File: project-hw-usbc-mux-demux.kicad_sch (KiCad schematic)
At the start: 0 parts

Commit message: sch: add buck converter
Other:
- added sheet Buck Converter (buck_converter.kicad_sch)
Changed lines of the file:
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@@
 	(generator_version "8.0")
 	(paper "A4")
+	(sheet
+		(at 38.735 38.1)
+		(size 14.605 12.7)
+		(fields_autoplaced yes)
+		(stroke
+			(width 0.1524)
+			(type solid)
+		)
+		(fill
+			(color 0 0 0 0.0000)
+		)
+		(property "Sheetname" "Buck Converter"
+			(at 38.735 37.3884 0)
+			(effects
+				(font
+					(size 1.27 1.27)
+				)
+				(justify left bottom)
+			)
+		)
+		(property "Sheetfile" "buck_converter.kicad_sch"
+			(at 38.735 51.3846 0)
+			(effects
+				(font
+					(size 1.27 1.27)
+				)
+				(justify left top)
+			)
+		)
+		(pin "5V" output
+			(at 53.34 40.64 0)
+			(effects
+				(font
+					(size 1.27 1.27)
+				)
+				(justify right)
+			)
+		)
+		(pin "Vin" input
+			(at 38.735 40.64 180)
+			(effects
+				(font
+					(size 1.27 1.27)
+				)
+				(justify left)
+			)
+		)
+		(pin "GND" input
+			(at 38.735 48.26 180)
+			(effects
+				(font
+					(size 1.27 1.27)
+				)
+				(justify left)
+			)
+		)
+		(instances
+			(project "project-hw-usbc-mux-demux"
+				(path "/a3c0ab3f-ca32-4edb-a5c1-d200028ec7dc"
+					(page "2")
+				)
+			)
+		)
+	)
 	(sheet_instances
 		(path "/"

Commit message: sch: first draft
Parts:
- added D1: LED_Small, LED_SMD:LED_0603_1608Metric, symbol Device:LED_Small
- added J1, J2, J3: Amphenol_12402012E212A, symbol Amphenol_12402012E212A:Amphenol_12402012E212A
- added R5, R6: 10k, Resistor_SMD:R_0603_1608Metric, symbol Device:R_Small
- added R7: 1k, Resistor_SMD:R_0603_1608Metric, symbol Device:R_Small
- added U2: FUSB303BTMX, QFN:Texas_X2QFN-12_1.6x1.6mm_P0.4mm, symbol onsemi_FUSB303BTMX:FUSB303BTMX
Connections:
- net Buck Converter/5V: now also R7.1
- new net: R6.1, U2.7 (SDA/OUT1)
- new net: J3.A5 (CC1), U2.1 (CC1)
- new net: J3.B5 (CC2), U2.2 (CC2)
- new net: J1.A5 (CC1), J2.A5 (CC1)
- new net: J1.B5 (CC2), J2.B5 (CC2)
- new net: R5.1, U2.8 (SCL/OUT2)
- new net: D1.2 (A), R7.2
- new net D+: J1.A6 (D+), J1.B6 (D+), J3.A6 (D+), J3.B6 (D+)
- new net D-: J1.A7 (D-), J1.B7 (D-), J3.A7 (D-), J3.B7 (D-)
- new net GND: D1.1 (K), J1.A1 (GND), J1.A12 (GND), J1.B1 (GND), J1.B12 (GND), J1.S1 (SHIELD), J2.A1 (GND), J2.A12 (GND), J2.B1 (GND), J2.B12 (GND), J2.S1 (SHIELD), J3.A1 (GND), J3.A12 (GND), J3.B1 (GND), J3.B12 (GND), J3.S1 (SHIELD), R5.2, R6.2, U2.10 (GND), U2.11 (~{EN})
- new net Load Switch/Out: J3.A4 (VBUS), J3.A9 (VBUS), J3.B4 (VBUS), J3.B9 (VBUS)
- new net VBUS_PD: J1.A4 (VBUS), J1.A9 (VBUS), J1.B4 (VBUS), J1.B9 (VBUS), J2.A4 (VBUS), J2.A9 (VBUS), J2.B4 (VBUS), J2.B9 (VBUS)
- no-connect marks 0 -> 13
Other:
- added sheet Load Switch (load_switch.kicad_sch)

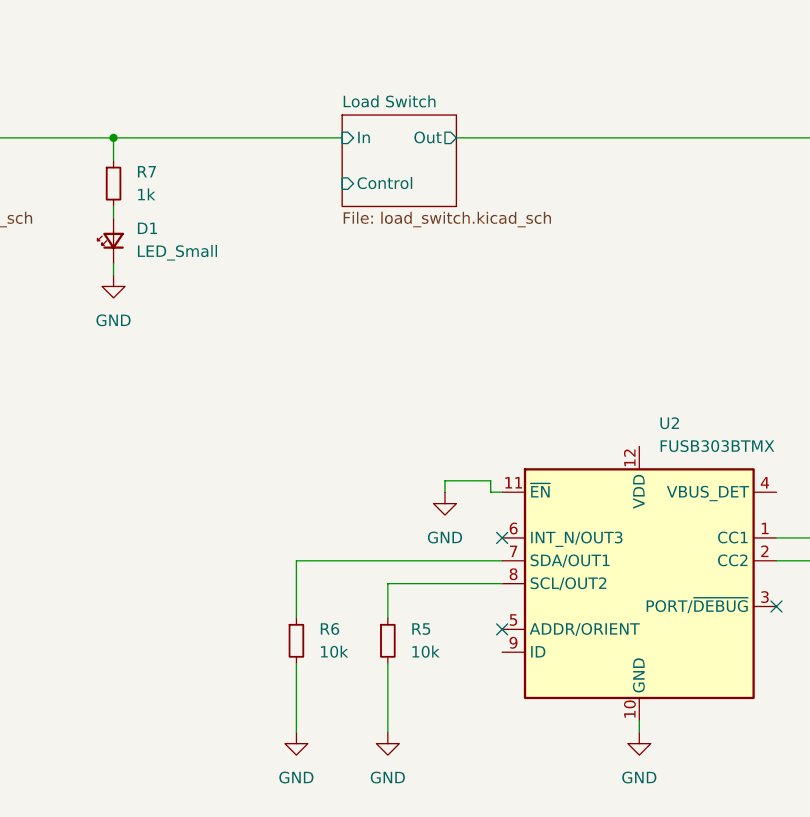
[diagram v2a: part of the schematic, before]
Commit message: sch: add zener diode
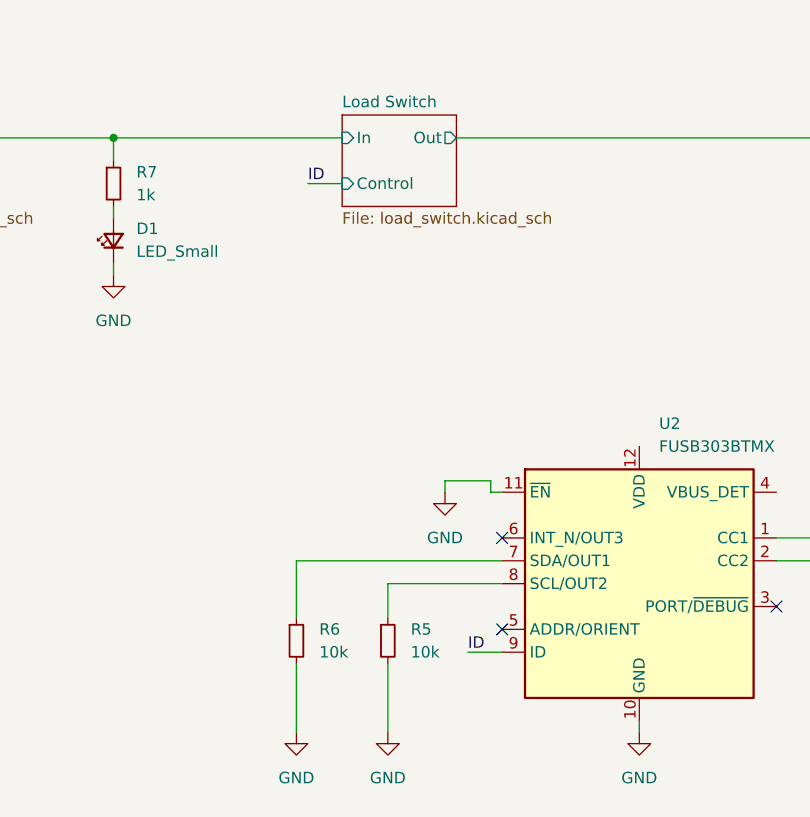
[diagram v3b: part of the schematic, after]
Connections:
- net ID: now reaches U2.9 (ID)
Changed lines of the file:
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@@
+	(wire
+		(pts
+			(xy 146.05 73.66) (xy 149.86 73.66)
+		)
+		(stroke
+			(width 0)
+			(type default)
+		)
+	)
 	(wire
 		(pts
@@
 		(pts
 			(xy 154.94 127) (xy 154.94 134.62)
+		)
+		(stroke
+			(width 0)
+			(type default)
+		)
+	)
+	(wire
+		(pts
+			(xy 163.83 125.73) (xy 167.64 125.73)
 		)
 		(stroke
@@
 		)
 	)
+	(label "ID"
+		(at 146.05 73.66 0)
+		(effects
+			(font
+				(size 1.27 1.27)
+			)
+			(justify left bottom)
+		)
+	)
+	(label "ID"
+		(at 163.83 125.73 0)
+		(effects
+			(font
+				(size 1.27 1.27)
+			)
+			(justify left bottom)
+		)
+	)

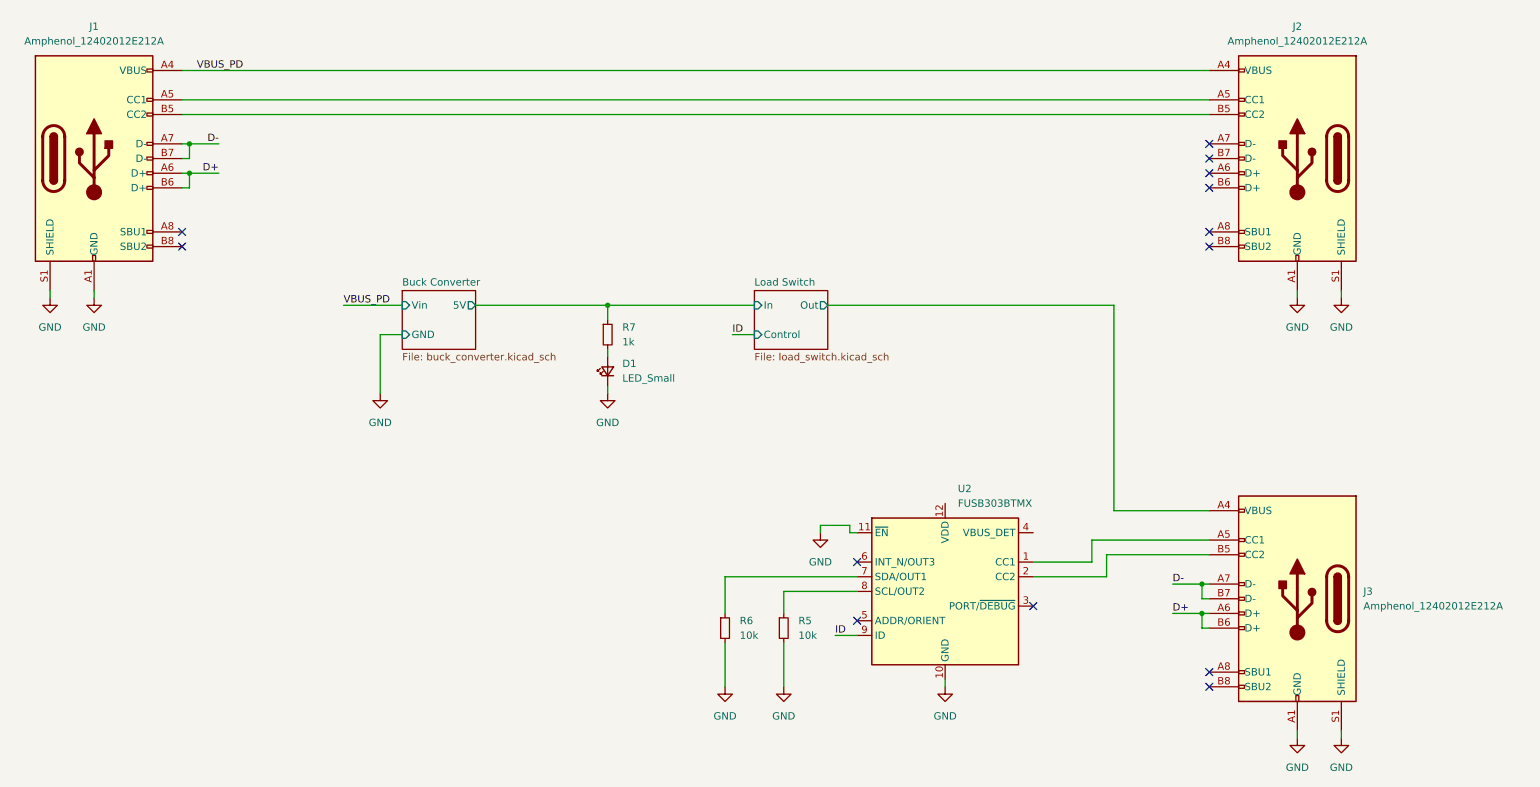
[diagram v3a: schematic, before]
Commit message: sch: fix errors
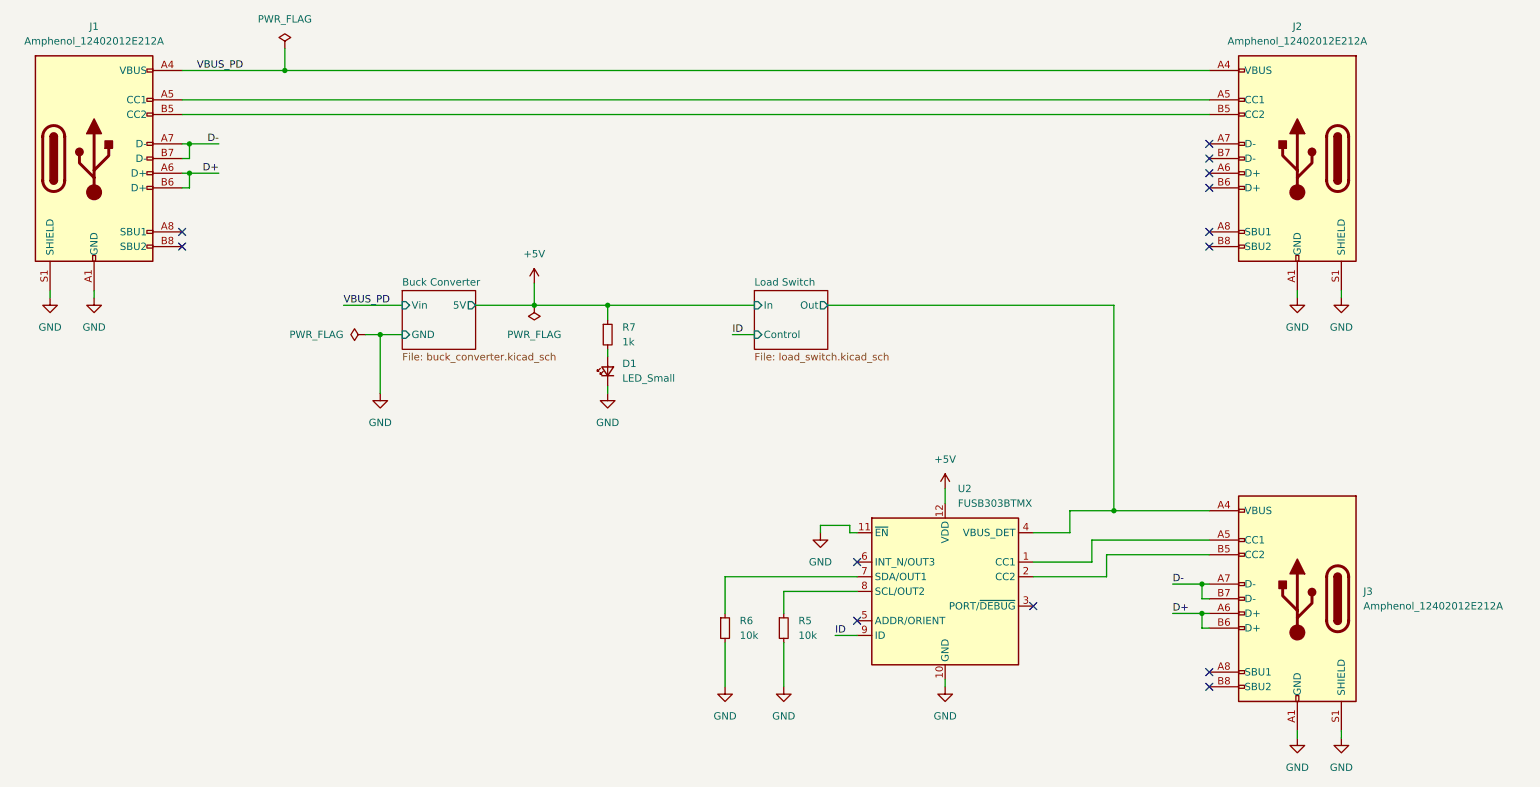
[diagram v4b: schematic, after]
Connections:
- net Buck Converter/5V is gone; now on net +5V: R7.1
- net Load Switch/Out: now also U2.4 (VBUS_DET)
- net +5V: now reaches U2.12 (VDD)

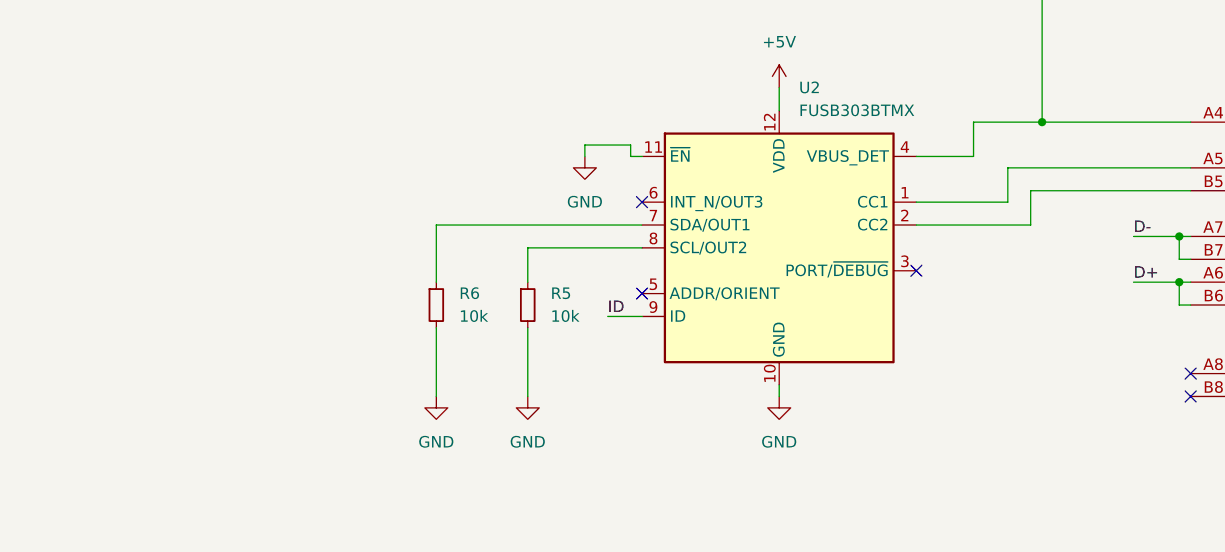
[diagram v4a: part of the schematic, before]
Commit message: sch: add test point
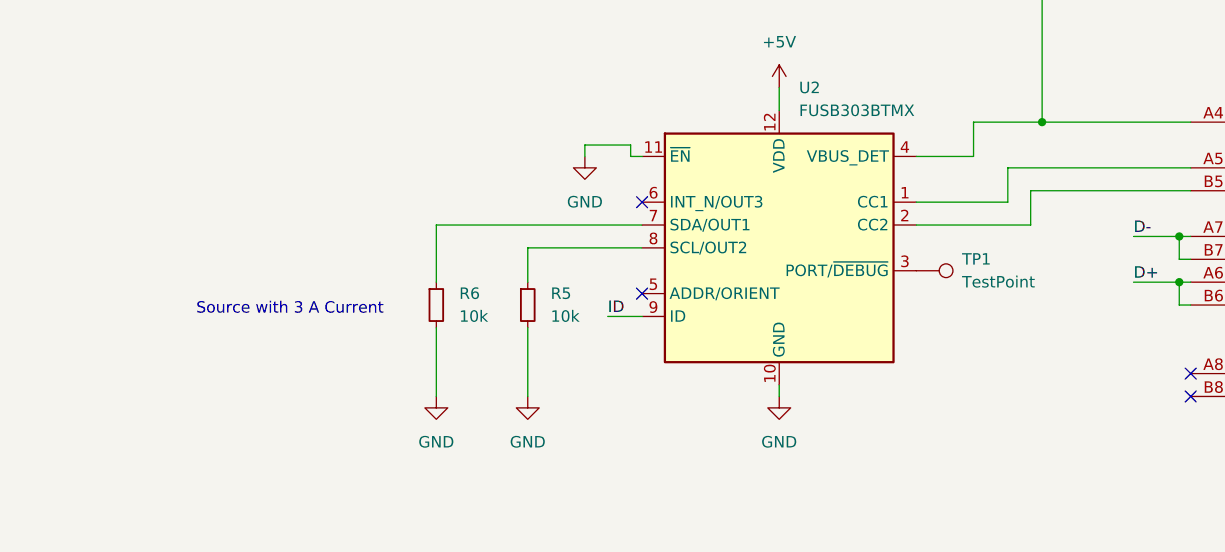
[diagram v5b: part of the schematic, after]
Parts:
- added TP1: TestPoint, TestPoint:TestPoint_Pad_D2.0mm, symbol Connector:TestPoint
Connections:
- net at U2.3 (PORT/~{DEBUG}): now also TP1.1
- no-connect marks 13 -> 12
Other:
- note added: "Source with 3 A Current"
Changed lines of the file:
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@@
-	)
-	(no_connect
-		(at 198.12 120.65)
 	)
 	(no_connect
@@
 			(width 0)
 			(type default)
+		)
+	)
+	(text "Source with 3 A Current"
+		(exclude_from_sim no)
+		(at 128.524 124.968 0)
+		(effects
+			(font
+				(size 1.27 1.27)
+			)
 		)
 	)
@@
 					(unit 1)
 				)
+			)
+		)
+	)
+	(symbol
+		(lib_id "Connector:TestPoint")
+		(at 198.12 120.65 270)
+		(unit 1)
+		(exclude_from_sim no)
+		(in_bom yes)
+		(on_board yes)
+		(dnp no)
+		(fields_autoplaced yes)
+		(property "Reference" "TP1"
+			(at 203.2 119.3799 90)
+			(effects
+				(font
+					(size 1.27 1.27)
+				)
+				(justify left)
+			)
+		)
+		(property "Value" "TestPoint"
+			(at 203.2 121.9199 90)
+			(effects
+				(font
+					(size 1.27 1.27)
+				)
+				(justify left)
+			)
+		)
+		(property "Footprint" "TestPoint:TestPoint_Pad_D2.0mm"
+			(at 198.12 125.73 0)
+			(effects
+				(font
+					(size 1.27 1.27)
+				)
+				(hide yes)
+			)
+		)
+		(property "Datasheet" "~"
+			(at 198.12 125.73 0)
+			(effects
+				(font
+					(size 1.27 1.27)
+				)
+				(hide yes)
+			)
+		)
+		(property "Description" "test point"
+			(at 198.12 120.65 0)
+			(effects
+				(font
+					(size 1.27 1.27)
+				)
+				(hide yes)
+			)
+		)
+		(pin "1"
+		)
+		(instances
+			(project ""
+				(path "/a3c0ab3f-ca32-4edb-a5c1-d200028ec7dc"
+					(reference "TP1")
+					(unit 1)
+				)

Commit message: sch: add usb footprint
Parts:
- J1, J2, J3: footprint (none) -> Connector_USB-C:Amphenol_12402012E212A
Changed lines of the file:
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@@
 			)
 		)
-		(property "Footprint" ""
+		(property "Footprint" "Connector_USB-C:Amphenol_12402012E212A"
 			(at 240.03 119.38 0)
 			(effects
@@
 			)
 		)
-		(property "Footprint" ""
+		(property "Footprint" "Connector_USB-C:Amphenol_12402012E212A"
 			(at 39.37 43.18 0)
 			(effects
@@
 			)
 		)
-		(property "Footprint" ""
+		(property "Footprint" "Connector_USB-C:Amphenol_12402012E212A"
 			(at 240.03 43.18 0)
 			(effects

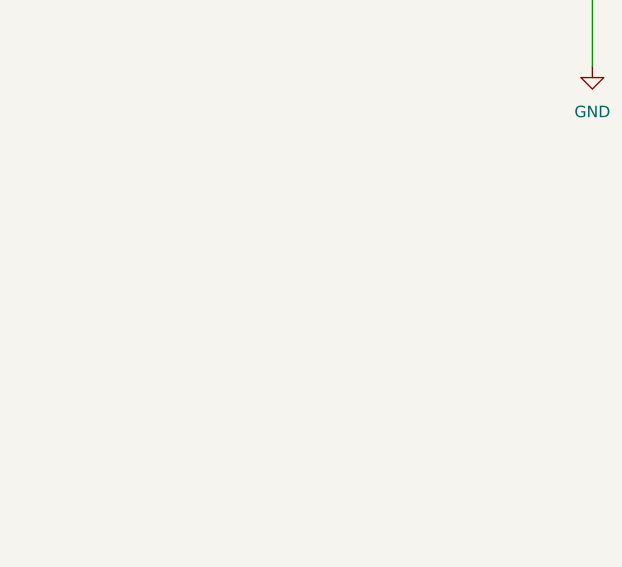
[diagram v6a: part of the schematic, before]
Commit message: sch: add power connectors
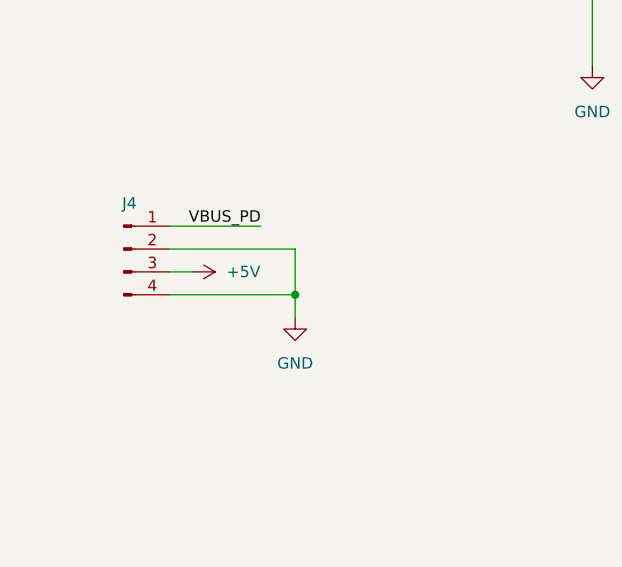
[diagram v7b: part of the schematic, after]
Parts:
- added J4: Conn_01x04_Pin, Connector_PinHeader_2.54mm:PinHeader_1x04_P2.54mm_Vertical, symbol Connector:Conn_01x04_Pin
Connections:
- net +5V: now also J4.3 (Pin_3)
- net GND: now also J4.2 (Pin_2), J4.4 (Pin_4)
- net VBUS_PD: now also J4.1 (Pin_1)

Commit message: pcb: route most of the board
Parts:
- TP1: footprint TestPoint:TestPoint_Pad_D2.0mm -> TestPoint:TestPoint_Pad_D1.0mm
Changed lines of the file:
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@@
 			)
 		)
-		(property "Footprint" "TestPoint:TestPoint_Pad_D2.0mm"
+		(property "Footprint" "TestPoint:TestPoint_Pad_D1.0mm"
 			(at 198.12 125.73 0)
 			(effects
